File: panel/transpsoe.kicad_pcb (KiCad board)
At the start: 2 copper layers, 106.3 x 39.6 mm, 15 parts

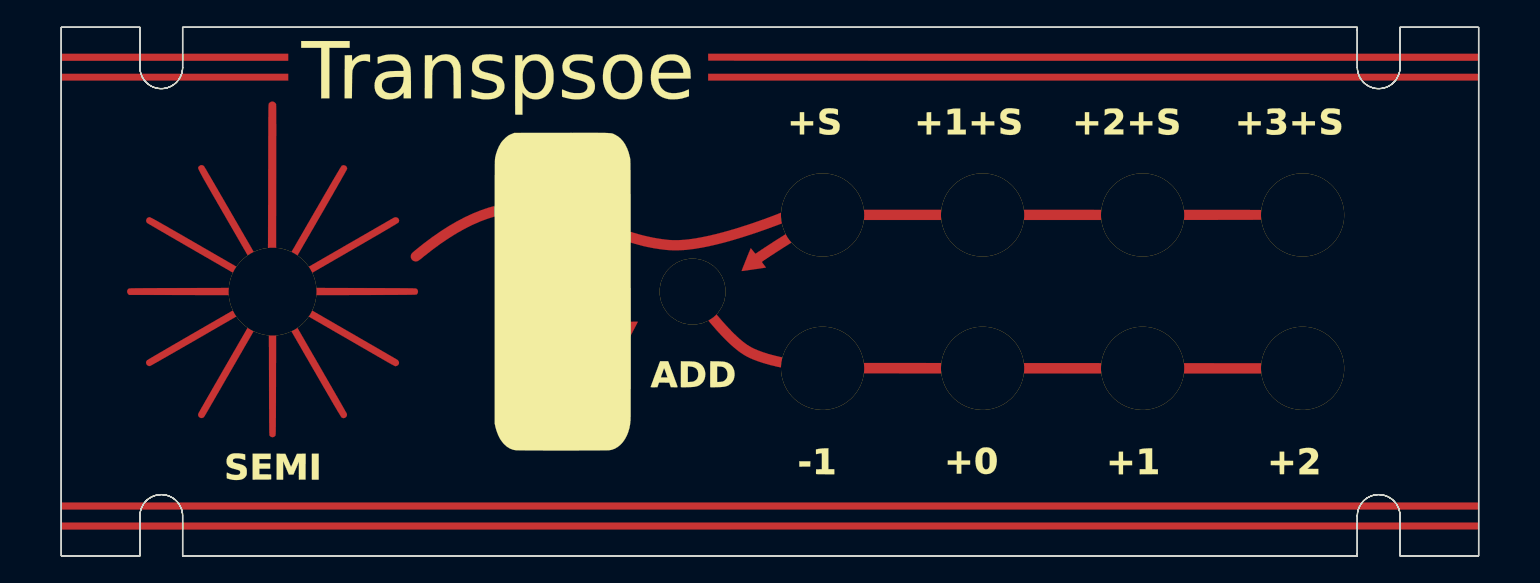
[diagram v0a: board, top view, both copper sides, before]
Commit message: Change fonts on panel
Also add a script for fixing up the panel to have
non-plated thru holes
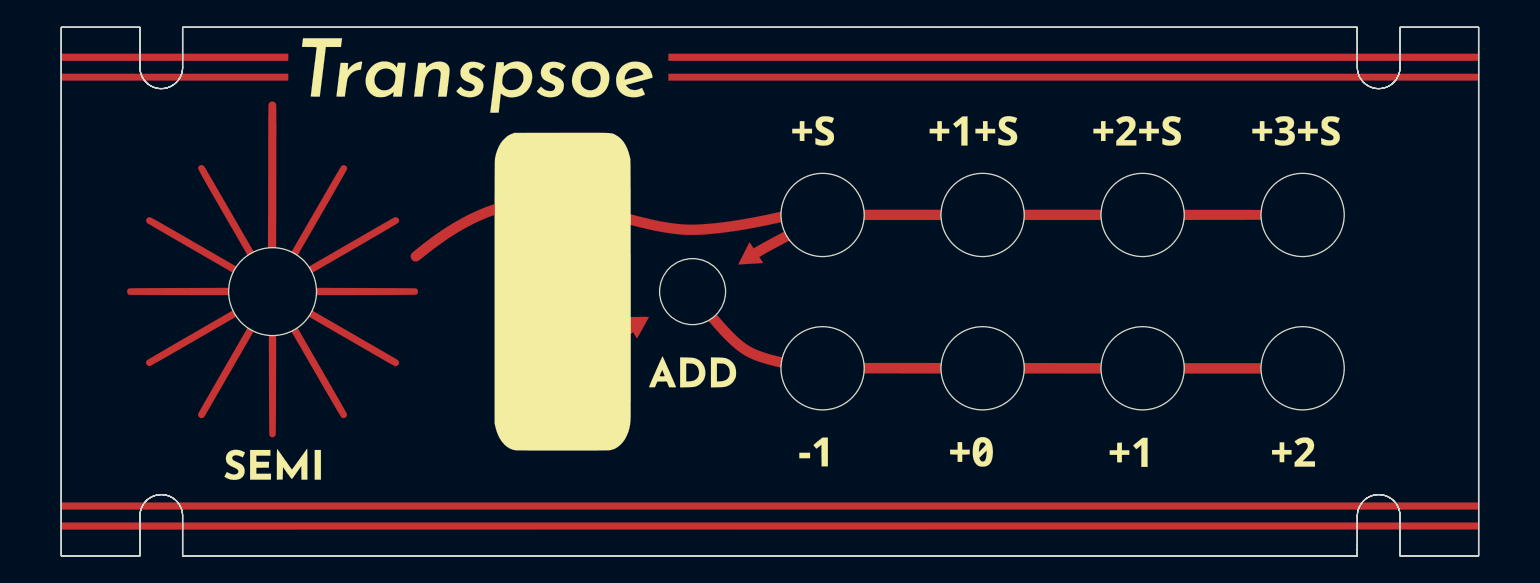
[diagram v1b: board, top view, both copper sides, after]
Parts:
- removed the G*** at (0.00, 0.00) (x3)
- added G*** (x3): LOGO, LOGO, F.Cu at (0.00, 0.00)

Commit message: Extend panel to 22hp to increase power cable clearance
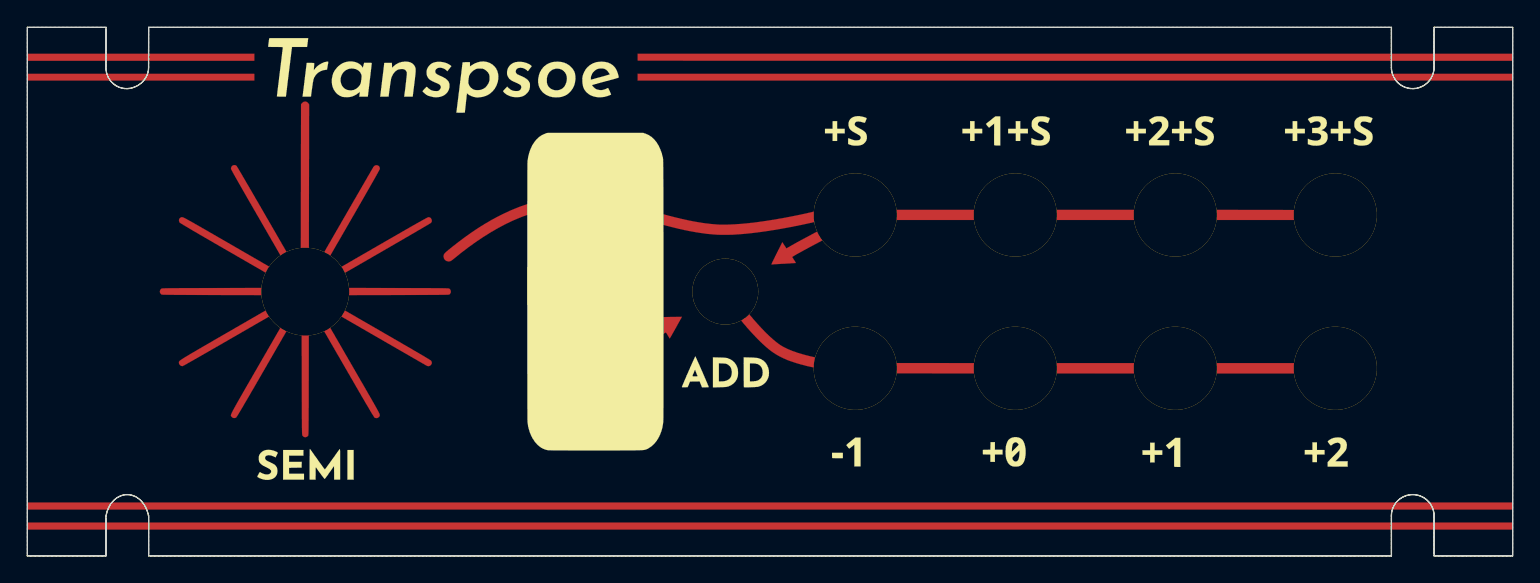
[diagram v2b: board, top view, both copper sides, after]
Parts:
- removed the ? at (39.9, 5.72)
- removed the ? at (-15.6, -5.78)
- removed the ? at (-37.3, -0.02)
- removed the ? at (-5.80, -0.02)
- removed the ? at (27.9, 5.72)
- removed the ? at (39.9, -5.78)
- removed the ? at (27.9, -5.78)
- removed the ? at (15.9, 5.72)
- removed the ? at (3.95, 5.72)
- removed the ? at (15.9, -5.78)
- removed the ? at (3.95, -5.78)
- removed the ? at (-15.6, 5.72)
- removed the G*** at (0.00, 0.00) (x3)
- added ?: , Wire_Pads:SolderWirePad_single_0-8mmDrill, F.Cu at (42.4, 5.72)
- added ?: , Wire_Pads:SolderWirePad_single_0-8mmDrill, F.Cu at (-13.1, -5.78)
- added ?: , Wire_Pads:SolderWirePad_single_0-8mmDrill, F.Cu at (-34.9, -0.02)
- added ?: , Wire_Pads:SolderWirePad_single_0-8mmDrill, F.Cu at (-3.35, -0.02)
- added ?: , Wire_Pads:SolderWirePad_single_0-8mmDrill, F.Cu at (30.4, 5.72)
- added ?: , Wire_Pads:SolderWirePad_single_0-8mmDrill, F.Cu at (42.4, -5.78)
- added ?: , Wire_Pads:SolderWirePad_single_0-8mmDrill, F.Cu at (30.4, -5.78)
- added ?: , Wire_Pads:SolderWirePad_single_0-8mmDrill, F.Cu at (18.4, 5.72)
- added ?: , Wire_Pads:SolderWirePad_single_0-8mmDrill, F.Cu at (6.40, 5.72)
- added ?: , Wire_Pads:SolderWirePad_single_0-8mmDrill, F.Cu at (18.4, -5.78)
- added ?: , Wire_Pads:SolderWirePad_single_0-8mmDrill, F.Cu at (6.40, -5.78)
- added ?: , Wire_Pads:SolderWirePad_single_0-8mmDrill, F.Cu at (-13.1, 5.72)
- added G*** (x3): LOGO, LOGO, F.Cu at (0.00, 0.00)
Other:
- board size 106.3 x 39.6 mm -> 111.4 x 39.6 mm

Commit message: Push 3.5mm jacks 0.05mm closer to the edge
It's a very small nudge, and puts them more at risk of being slightly
off the board, but increases the tolerances for clearance between
adjacent jacks. We have ~0.5mm of clearance on the side of the board,
and this should only eat into at most 0.1mm of it.
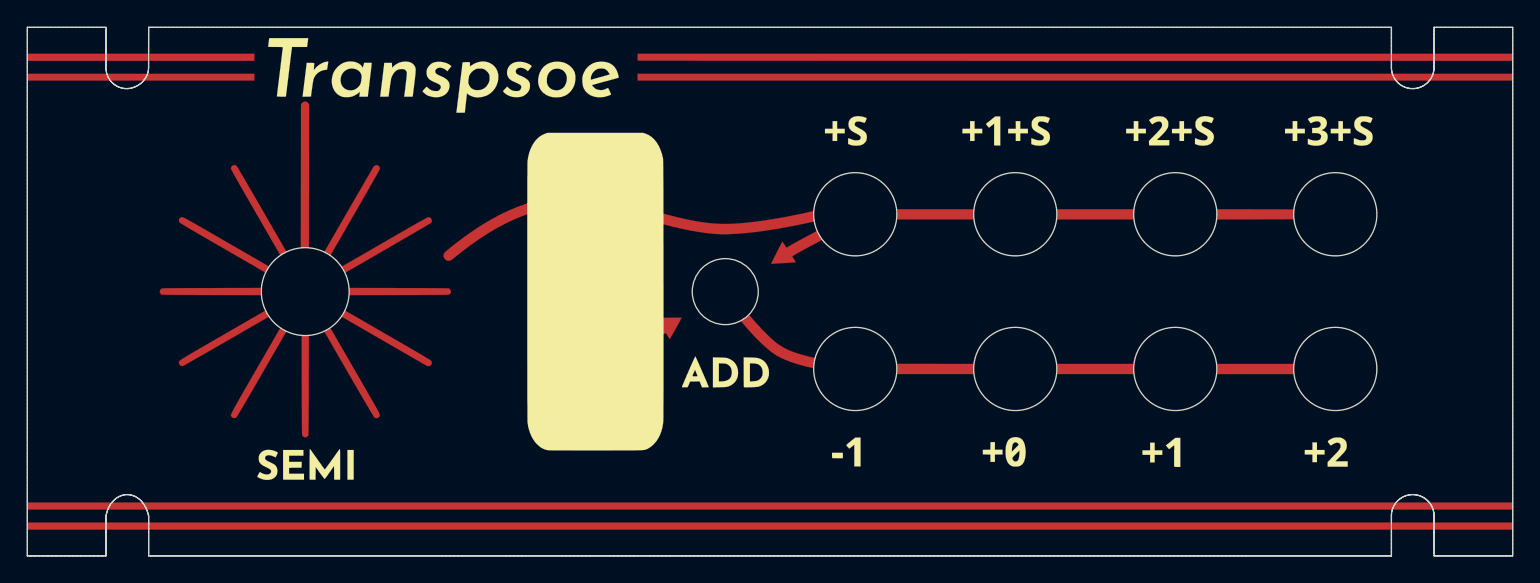
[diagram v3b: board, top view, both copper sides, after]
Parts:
- removed the ? at (42.4, 5.72)
- removed the ? at (-13.1, -5.78)
- removed the ? at (30.4, 5.72)
- removed the ? at (42.4, -5.78)
- removed the ? at (30.4, -5.78)
- removed the ? at (18.4, 5.72)
- removed the ? at (6.40, 5.72)
- removed the ? at (18.4, -5.78)
- removed the ? at (6.40, -5.78)
- removed the ? at (-13.1, 5.72)
- removed the G*** at (0.00, 0.00) (x3)
- added ?: , Wire_Pads:SolderWirePad_single_0-8mmDrill, F.Cu at (42.4, 5.77)
- added ?: , Wire_Pads:SolderWirePad_single_0-8mmDrill, F.Cu at (-13.1, -5.83)
- added ?: , Wire_Pads:SolderWirePad_single_0-8mmDrill, F.Cu at (30.4, 5.77)
- added ?: , Wire_Pads:SolderWirePad_single_0-8mmDrill, F.Cu at (42.4, -5.83)
- added ?: , Wire_Pads:SolderWirePad_single_0-8mmDrill, F.Cu at (30.4, -5.83)
- added ?: , Wire_Pads:SolderWirePad_single_0-8mmDrill, F.Cu at (18.4, 5.77)
- added ?: , Wire_Pads:SolderWirePad_single_0-8mmDrill, F.Cu at (6.40, 5.77)
- added ?: , Wire_Pads:SolderWirePad_single_0-8mmDrill, F.Cu at (18.4, -5.83)
- added ?: , Wire_Pads:SolderWirePad_single_0-8mmDrill, F.Cu at (6.40, -5.83)
- added ?: , Wire_Pads:SolderWirePad_single_0-8mmDrill, F.Cu at (-13.1, 5.77)
- added G*** (x3): LOGO, LOGO, F.Cu at (0.00, 0.00)
